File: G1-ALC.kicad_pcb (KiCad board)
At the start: 2 copper layers, 100 x 100.1 mm, 89 parts, among them J101 Conn_01x03_Pin, J102 330 VAC In, J103 G1 conn., J104 105VAC in, J105 Conn_01x03_Pin, J107 Conn_01x05_Pin, J108 G2 Control board interconnect, Q101 TIP122, U101 LM7812_TO220, U102 LM324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

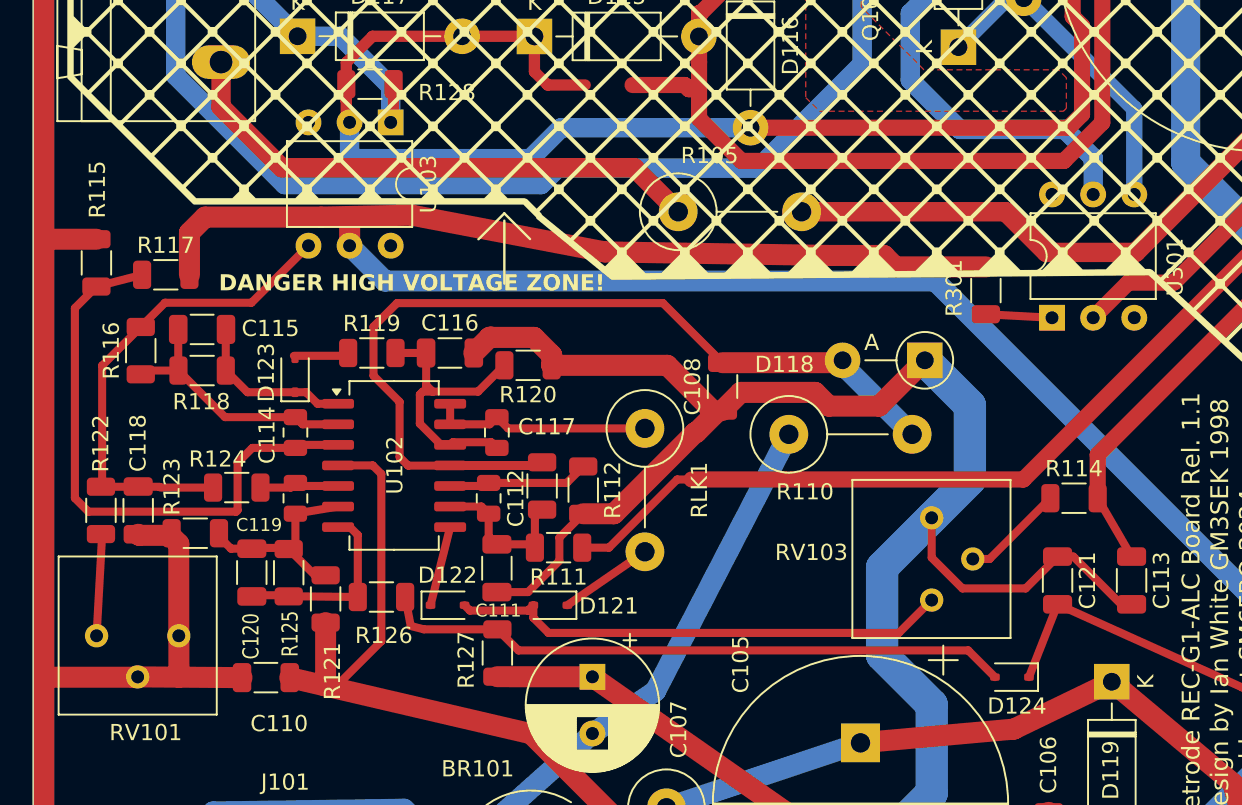
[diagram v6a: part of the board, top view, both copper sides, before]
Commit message: Moved cold end of R115 to CLASS_AB1_L instead of GND. The intent is to turn off ALC in case we want to run the PA in class C.
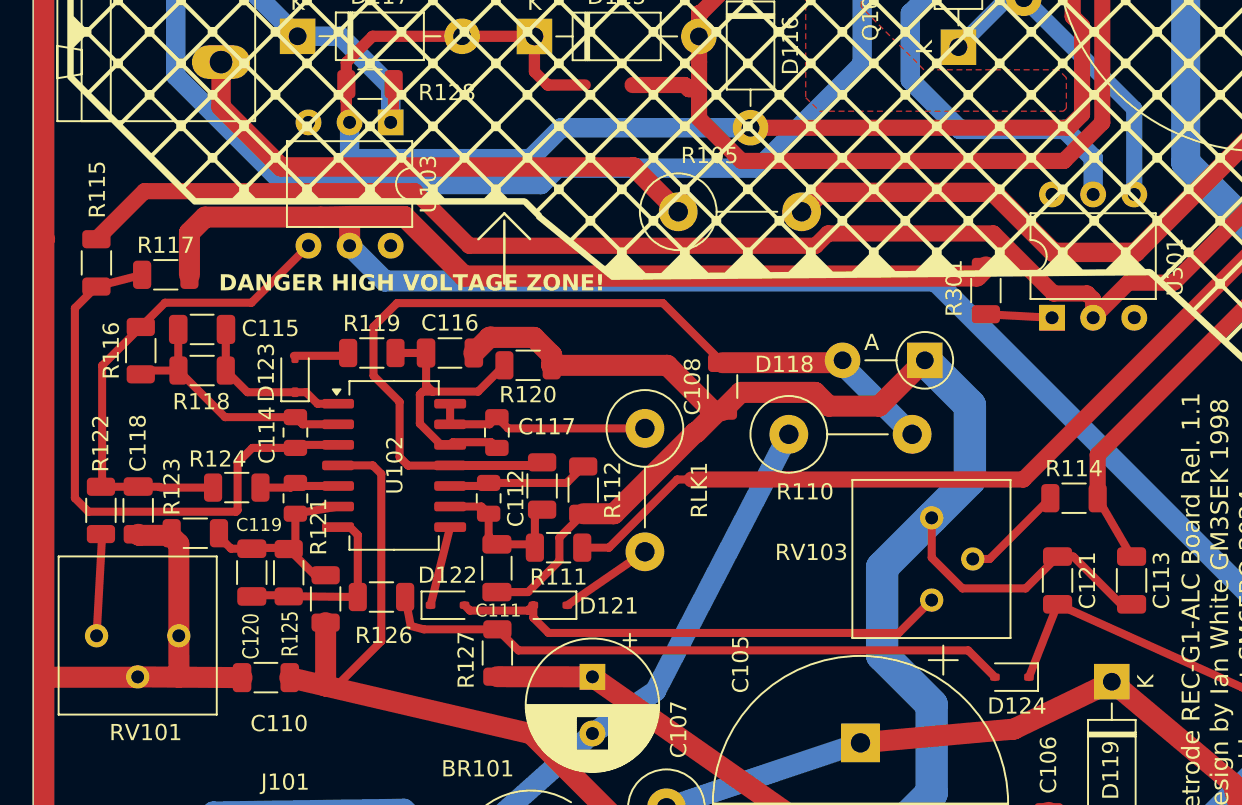
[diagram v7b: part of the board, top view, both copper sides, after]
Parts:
- turned R121 to -90 degrees
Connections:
- R115 pad 1: GNDPWR -> /Class AB1_L
- R121 pad 1: +12V Reg -> Net-(U102B--)
- R121 pad 2: Net-(U102B--) -> +12V Reg
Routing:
- net /Class AB1_L: track 45.9 -> 113.2 mm
- net GNDPWR: track 992.8 -> 989.6 mm
- net +12V Reg: track 285.2 -> 286.4 mm
- net Net-(C103-Pad2): track 81.2 -> 82.2 mm
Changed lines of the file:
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@@
 	(footprint "Resistor_SMD:R_1206_3216Metric"
 		(layer "F.Cu")
-		(at 68.1 101.67 90)
+		(at 68.1 101.67 -90)
 		(descr "Resistor SMD 1206 (3216 Metric), square (rectangular) end terminal, IPC_7351 nominal, (Body size source: IPC-SM-782 page 72, https://www.pcb-3d.com/wordpress/wp-content/uploads/ipc-sm-782a_amendment_1_and_2.pdf), generated with kicad-footprint-generator")
 		(tags "resistor")
@@
 		)
 		(property "Footprint" "Resistor_SMD:R_1206_3216Metric"
-			(at 0 0 90)
+			(at 0 0 -90)
 			(unlocked yes)
 			(layer "F.Fab")
@@
 		)
 		(property "Datasheet" ""
-			(at 0 0 90)
+			(at 0 0 -90)
 			(unlocked yes)
 			(layer "F.Fab")
@@
 		)
 		(property "Description" ""
-			(at 0 0 90)
+			(at 0 0 -90)
 			(unlocked yes)
 			(layer "F.Fab")
@@
 		)
 		(property "Notes" ""
-			(at 0 0 0)
+			(at 0 0 180)
 			(layer "F.Fab")
 			(hide yes)
@@
 		)
 		(property "Order #" "40818410"
-			(at 0 0 0)
+			(at 0 0 180)
 			(layer "F.Fab")
 			(hide yes)
@@
 		)
 		(property "Supplier" "Electrokit"
-			(at 0 0 0)
+			(at 0 0 180)
 			(layer "F.Fab")
 			(hide yes)
@@
 		(attr smd)
 		(fp_line
-			(start -0.727064 -0.91)
-			(end 0.727064 -0.91)
+			(start -0.727064 0.91)
+			(end 0.727064 0.91)
 			(stroke
 				(width 0.12)
@@
 		)
 		(fp_line
-			(start -0.727064 0.91)
-			(end 0.727064 0.91)
+			(start -0.727064 -0.91)
+			(end 0.727064 -0.91)
 			(stroke
 				(width 0.12)
@@
 		)
 		(fp_line
-			(start 2.28 -1.12)
-			(end 2.28 1.12)
+			(start -2.28 1.12)
+			(end -2.28 -1.12)
 			(stroke
 				(width 0.05)
@@
 		)
 		(fp_line
-			(start -2.28 -1.12)
-			(end 2.28 -1.12)
+			(start 2.28 1.12)
+			(end -2.28 1.12)
 			(stroke
 				(width 0.05)
@@
 		)
 		(fp_line
-			(start 2.28 1.12)
-			(end -2.28 1.12)
+			(start -2.28 -1.12)
+			(end 2.28 -1.12)
 			(stroke
 				(width 0.05)
@@
 		)
 		(fp_line
-			(start -2.28 1.12)
-			(end -2.28 -1.12)
+			(start 2.28 -1.12)
+			(end 2.28 1.12)
 			(stroke
 				(width 0.05)
@@
 		)
 		(fp_line
-			(start 1.6 -0.8)
-			(end 1.6 0.8)
+			(start -1.6 0.8)
+			(end -1.6 -0.8)
 			(stroke
 				(width 0.1)
@@
 		)
 		(fp_line
-			(start -1.6 -0.8)
-			(end 1.6 -0.8)
+			(start 1.6 0.8)
+			(end -1.6 0.8)
 			(stroke
 				(width 0.1)
@@
 		)
 		(fp_line
-			(start 1.6 0.8)
-			(end -1.6 0.8)
+			(start -1.6 -0.8)
+			(end 1.6 -0.8)
 			(stroke
 				(width 0.1)
@@
 		)
 		(fp_line
-			(start -1.6 0.8)
-			(end -1.6 -0.8)
+			(start 1.6 -0.8)
+			(end 1.6 0.8)
 			(stroke
 				(width 0.1)
@@
 		)
 		(pad "1" smd roundrect
-			(at -1.4625 0 90)
+			(at -1.4625 0 270)
 			(size 1.125 1.75)
 			(layers "F.Cu" "F.Paste" "F.Mask")
 			(roundrect_rratio 0.2222222222)
-			(net 10 "+12V Reg")
+			(net 24 "Net-(U102B--)")
 			(pintype "passive")
 		)
 		(pad "2" smd roundrect
-			(at 1.4625 0 90)
+			(at 1.4625 0 270)
 			(size 1.125 1.75)
 			(layers "F.Cu" "F.Paste" "F.Mask")
 			(roundrect_rratio 0.2222222222)
-			(net 24 "Net-(U102B--)")
+			(net 10 "+12V Reg")
 			(pintype "passive")
 		)
@@
 			(layers "F.Cu" "F.Paste" "F.Mask")
 			(roundrect_rratio 0.2222222222)
-			(net 11 "GNDPWR")
+			(net 49 "/Class AB1_L")
 			(pintype "passive")
 		)
@@
 	)
 	(segment
-		(start 97.505 77.75)
-		(end 110.11 77.75)
+		(start 130.839775 61.384316)
+		(end 130.839775 47.630225)
 		(width 1.2)
 		(layer "F.Cu")
@@
 	)
 	(segment
-		(start 130.839775 61.384316)
-		(end 130.839775 47.630225)
+		(start 130.999775 47.630225)
+		(end 133.46 45.17)
 		(width 1.2)
 		(layer "F.Cu")
@@
 	)
 	(segment
-		(start 130.999775 47.630225)
-		(end 133.46 45.17)
+		(start 113.06132 80.26)
+		(end 118.14 80.26)
 		(width 1.2)
 		(layer "F.Cu")
@@
 	)
 	(segment
-		(start 110.11 77.75)
-		(end 112.62 80.26)
+		(start 97.505 77.75)
+		(end 98.705 76.55)
 		(width 1.2)
 		(layer "F.Cu")
@@
 	)
 	(segment
-		(start 118.14 80.26)
-		(end 130.839775 67.560225)
+		(start 109.35132 76.55)
+		(end 113.06132 80.26)
+		(width 1.2)
+		(layer "F.Cu")
+		(net 8)
+	)
+	(segment
+		(start 98.705 76.55)
+		(end 109.35132 76.55)
 		(width 1.2)
 		(layer "F.Cu")
@@
 	)
 	(segment
-		(start 112.62 80.26)
-		(end 118.14 80.26)
+		(start 118.14 80.26)
+		(end 130.839775 67.560225)
 		(width 1.2)
 		(layer "F.Cu")
@@
 	)
 	(segment
-		(start 102.587732 80.45)
-		(end 103.295232 81.1575)
-		(width 1.3)
-		(layer "F.Cu")
-		(net 10)
-	)
-	(segment
 		(start 115.805476 117.807)
 		(end 116.669476 116.943)
@@
 	(segment
 		(start 69.59 78.041598)
-		(end 73.42 77.96)
+		(end 72.969567 78.041598)
 		(width 1.3)
 		(layer "F.Cu")
@@
 	)
 	(segment
+		(start 72.969567 78.041598)
+		(end 76.647969 81.72)
+		(width 1.3)
+		(layer "F.Cu")
+		(net 10)
+	)
+	(segment
 		(start 112.776 117.807)
 		(end 115.805476 117.807)
@@
 	)
 	(segment
+		(start 108.3275 81.72)
+		(end 108.89 81.1575)
+		(width 1.3)
+		(layer "F.Cu")
+		(net 10)
+	)
+	(segment
 		(start 68.1 103.1325)
 		(end 68.1 107.045669)
@@
 	)
 	(segment
-		(start 73.42 77.96)
-		(end 85.34 80.23)
+		(start 76.647969 81.72)
+		(end 108.3275 81.72)
 		(width 1.3)
 		(layer "F.Cu")
@@
 	)
 	(segment
-		(start 99.33 80.45)
-		(end 102.587732 80.45)
-		(width 1.3)
-		(layer "F.Cu")
-		(net 10)
-	)
-	(segment
-		(start 85.34 80.23)
-		(end 99.33 80.45)
-		(width 1.3)
-		(layer "F.Cu")
-		(net 10)
-	)
-	(segment
-		(start 103.295232 81.1575)
-		(end 108.89 81.1575)
-		(width 1.3)
-		(layer "F.Cu")
-		(net 10)
-	)
-	(segment
 		(start 137.11 98.32)
 		(end 143.2975 98.32)
@@
 	)
 	(segment
-		(start 53.94 79.447367)
-		(end 50.738633 79.447367)
-		(width 1.3)
-		(layer "F.Cu")
-		(net 11)
-	)
-	(segment
 		(start 116 124.426)
 		(end 144.824 124.426)
@@
 	)
 	(segment
-		(start 87.165 75.03)
-		(end 89.885 77.75)
+		(start 61.6387 68.5038)
+		(end 61.6387 71.2687)
 		(width 1.2)
 		(layer "F.Cu")
@@
 	)
 	(segment
-		(start 65.4 75.03)
-		(end 87.165 75.03)
+		(start 87.115 74.98)
+		(end 89.885 77.75)
 		(width 1.2)
 		(layer "F.Cu")
@@
 	)
 	(segment
-		(start 61.6387 68.5038)
-		(end 61.6387 71.2687)
+		(start 65.35 74.98)
+		(end 87.115 74.98)
 		(width 1.2)
 		(layer "F.Cu")
@@
 	(segment
 		(start 61.6387 71.2687)
-		(end 65.4 75.03)
+		(end 65.35 74.98)
 		(width 1.2)
 		(layer "F.Cu")
@@
 	)
 	(segment
+		(start 113.07 82.8)
+		(end 109.362425 79.092425)
+		(width 1)
+		(layer "F.Cu")
+		(net 49)
+	)
+	(segment
+		(start 115.515 84.3)
+		(end 115.515 83.16863)
+		(width 1)
+		(layer "F.Cu")
+		(net 49)
+	)
+	(segment
+		(start 98.374849 79.85)
+		(end 76.97 79.85)
+		(width 1)
+		(layer "F.Cu")
+		(net 49)
+	)
+	(segment
 		(start 135.62 67.01)
 		(end 120.5 82.13)
@@
 	)
 	(segment
+		(start 76.97 79.85)
+		(end 73.6 76.48)
+		(width 1)
+		(layer "F.Cu")
+		(net 49)
+	)
+	(segment
+		(start 115.515 83.16863)
+		(end 115.14637 82.8)
+		(width 1)
+		(layer "F.Cu")
+		(net 49)
+	)
+	(segment
+		(start 115.14637 82.8)
+		(end 113.07 82.8)
+		(width 1)
+		(layer "F.Cu")
+		(net 49)
+	)
+	(segment
+		(start 56.907367 76.48)
+		(end 53.94 79.447367)
+		(width 1)
+		(layer "F.Cu")
+		(net 49)
+	)
+	(segment
 		(start 138.77 54.3)
 		(end 135.62 57.45)
@@
 	)
 	(segment
+		(start 73.6 76.48)
+		(end 56.907367 76.48)
+		(width 1)
+		(layer "F.Cu")
+		(net 49)
+	)
+	(segment
+		(start 109.362425 79.092425)
+		(end 99.132424 79.092425)
+		(width 1)
+		(layer "F.Cu")
+		(net 49)
+	)
+	(segment
 		(start 120.5 82.13)
 		(end 117.685 82.13)
@@
 		(width 1)
 		(layer "F.Cu")
+		(net 49)
+	)
+	(segment
+		(start 99.132424 79.092425)
+		(end 98.374849 79.85)
+		(width 1)
+		(layer "F.Cu")

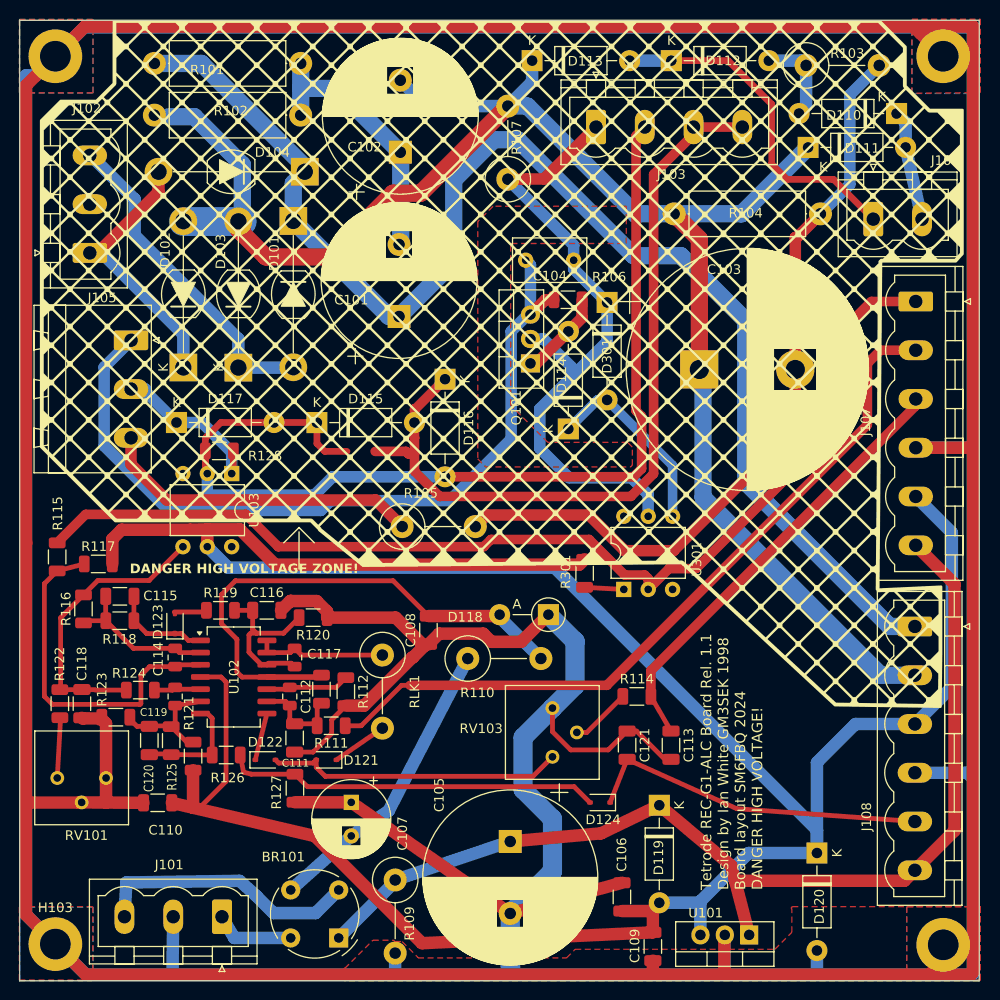
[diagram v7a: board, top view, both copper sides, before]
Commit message: Updated format to KiCad 9. Included footprints etc.
Standardized PCB layers, updated property formatting, and adjusted net assignments. Added some DigiKey, Electrokit, and Mouser component part numbers.
Reduced font sizes for better readability and incorporated embedded font settings.
Removed the sequencer from the schematic which wasn't really meant to be there.
Revised and excluded drc and erc warnings and exclusions.
Included footprints into the project library that formerly was defined outside of the project.
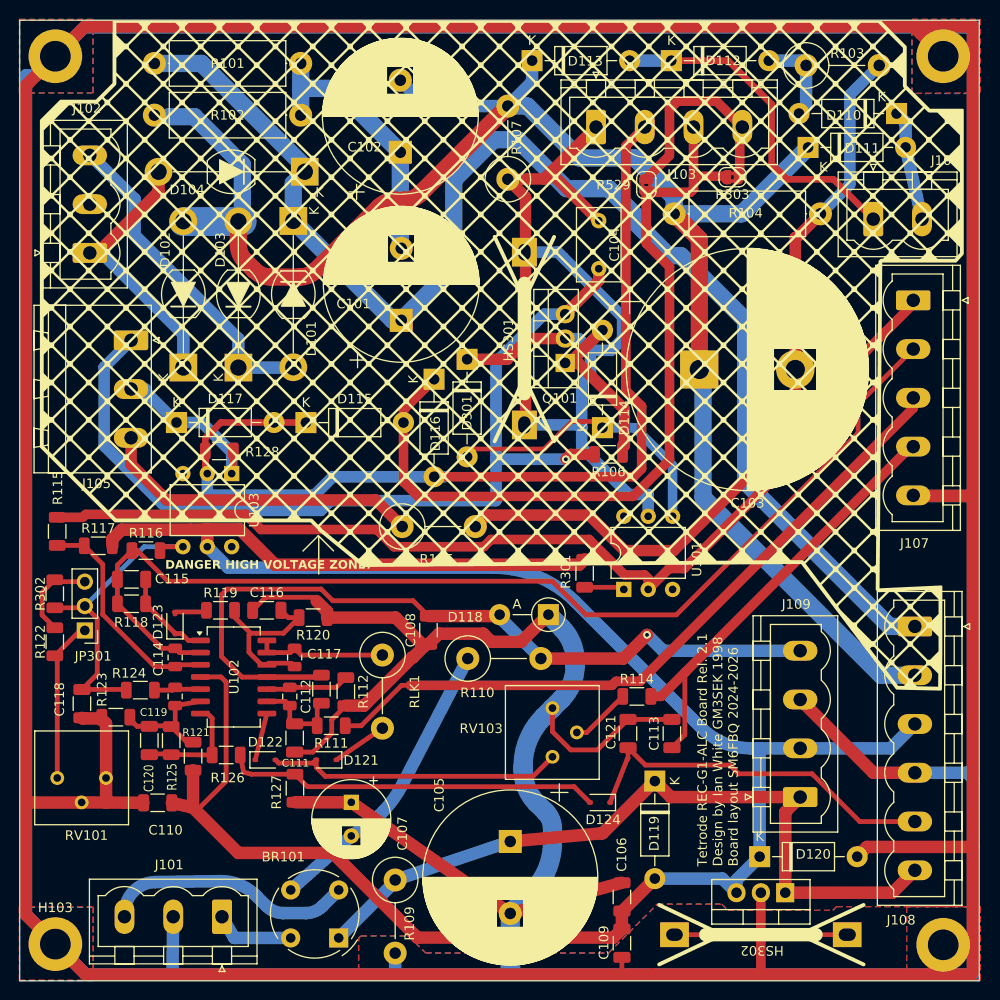
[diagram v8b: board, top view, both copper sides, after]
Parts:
- added HS301: Heatsink_Pad_2Pin, Project_library:6025DG_Cooler, F.Cu at (102.6, 58.2)
- added HS302: Heatsink_Pad_2Pin, Project_library:6025DG_Cooler, F.Cu at (127.3, 120.3)
- added J109: G1 conn., Connector_Phoenix_MSTB:PhoenixContact_MSTBVA_2,5_4-G-5,08_1x04_P5.08mm_Vertical, F.Cu at (131.3, 105.9)
- added JP301: ALC tune, Connector_PinHeader_2.54mm:PinHeader_1x03_P2.54mm_Vertical, F.Cu at (56.8, 88.6)
- added R302: 560R, Resistor_SMD:R_1206_3216Metric, F.Cu at (53.7, 84.8)
- added R303: 0, Jumper:SolderJumper-2_P1.3mm_Bridged2Bar_RoundedPad1.0x1.5mm, F.Cu at (124.3, 41.4)
- added R529: 0, Jumper:SolderJumper-2_P1.3mm_Bridged2Bar_RoundedPad1.0x1.5mm, F.Cu at (115.3, 42.2)
- D101, D102, D103, D104: footprint Diode_THT_AKL:D_SOD-64_P15.24mm_big_holes_Horizontal -> Project_library:D_SOD-64_P15.24mm_big_holes_Horizontal
- J102: value 330 VAC In -> 330VAC
- J107: footprint Connector_Phoenix_MSTB:PhoenixContact_MSTBVA_2,5_6-G-5,08_1x06_P5.08mm_Vertical -> Connector_Phoenix_MSTB:PhoenixContact_MSTBVA_2,5_5-G-5,08_1x05_P5.08mm_Vertical
- Q101, U101: footprint Package_TO_SOT_THT:TO-220-3_Vertical_Cooler -> Package_TO_SOT_THT:TO-220-3_Vertical
- R126: value 100k -> 39k
- moved R106 16.7 mm to (111.4, 70.2)
- moved D301 15.7 mm to (96.6, 60.3)
- moved R116 8.91 mm to (63.2, 80.3), turned to 0 degrees
- moved R122 6.47 mm to (53.7, 89.8)
- moved D120 5.98 mm to (127.1, 112.1), turned to 0 degrees
- moved U101 5.79 mm to (129.8, 115.9)
- moved C104 4.87 mm to (110.4, 45.9), turned to -90 degrees
- moved Q101 3.61 mm to (106.9, 60.7)
- moved D114 3.56 mm to (110.7, 67.5)
- moved C109 3.24 mm to (112.8, 121.2)
- moved R115 2.66 mm to (53.9, 78.3)
- moved D119 2.56 mm to (116.2, 104.3)
- moved C115 2.15 mm to (61.7, 83.3)
- moved R118 2.15 mm to (61.7, 85.8)
- moved R117 1.89 mm to (58.2, 79.8)
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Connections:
- C105 pad 2: GNDPWR -> GND
- C106 pad 1: +12V Reg -> +12V
- C106 pad 2: GNDPWR -> GND
- C107 pad 1: GNDPWR -> GND
- C108 pad 1: GNDPWR -> GND
- C109 pad 1: +12V Reg -> +12V
- C109 pad 2: GNDPWR -> GND
- C110 pad 1: +12V Reg -> +12V
- C110 pad 2: GNDPWR -> GND
- C111 pad 2: GNDPWR -> GND
- C113 pad 2: GNDPWR -> GND
- C114 pad 2: Net-(U102A--) -> /Ig1
- C115 pad 1: Net-(U102A--) -> /Ig1
- C116 pad 1: Net-(U102D-+) -> GND
- C116 pad 2: GNDPWR -> Net-(U102D-+)
- C118 pad 1: Net-(C118-Pad1) -> Net-(JP301-C)
- C118 pad 2: GNDPWR -> GND
- C121 pad 1: GNDPWR -> GND
- D115 pad 2: /G1 -> /G1 meter -
- D116 pad 1: /G1 -> /G1 meter -
- D118 pad 1: GNDPWR -> GND
- D119 pad 2: +12V Reg -> +12V
- D120 pad 1: +12V Reg -> +12V
- D120 pad 2: GNDPWR -> GND
- H101 pad 1: GNDPWR -> GND
- H102 pad 1: GNDPWR -> GND
- H103 pad 1: GNDPWR -> GND
- H104 pad 1: GNDPWR -> GND
- J101 pad 2: GNDPWR -> GND
- J103 pad 3: /G1 -> /G1 meter -
- J107 pad 2: /Inhibit -> /Ig1
- J107 pad 3: /ALC -> /Inhibit
- J107 pad 4: GNDPWR -> /ALC
- J107 pad 5: +12V Reg -> GND
- J108 pad 3: +12V Reg -> +12V
- J108 pad 4: GNDPWR -> GND
- R109 pad 2: GNDPWR -> GND
- R112 pad 2: GNDPWR -> GND
- R116 pad 1: Net-(U102A--) -> /Ig1
- R116 pad 2: Net-(C118-Pad1) -> Net-(JP301-C)
- R117 pad 2: +12V Reg -> +12V
- R118 pad 1: Net-(U102A--) -> /Ig1
- R120 pad 1: GNDPWR -> GND
- R121 pad 2: +12V Reg -> +12V
- R122 pad 1: Net-(C118-Pad1) -> Net-(JP301-B)
- R123 pad 1: GNDPWR -> GND
- R124 pad 1: Net-(C118-Pad1) -> Net-(JP301-C)
- R127 pad 1: GNDPWR -> GND
- R301 pad 1: +12V Reg -> +12V
- RV101 pad 2: GNDPWR -> GND
- RV101 pad 3: GNDPWR -> GND
- RV103 pad 3: GNDPWR -> GND
- U101 pad 2: GNDPWR -> GND
- U101 pad 3: +12V Reg -> +12V
- U102 pad 2: Net-(U102A--) -> /Ig1
- U102 pad 4: +12V Reg -> +12V
- U103 pad 4: Net-(C118-Pad1) -> Net-(JP301-C)
- U103 pad 5: +12V Reg -> +12V
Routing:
- net GND: track 0.00 -> 1035.4 mm
- net GNDPWR: track 989.6 -> 0.00 mm
- net +12V Reg: track 286.4 -> 0.00 mm
- net +12V: track 0.00 -> 242.0 mm
- net /Ig1: track 0.00 -> 114.3 mm
- net /G1 meter -: track 0.00 -> 85.8 mm
- net /G1: track 84.4 -> 22.6 mm
- net /G1 Switch: track 68.8 -> 106.1 mm
- net Net-(JP301-C): track 0.00 -> 33.7 mm
- net +24V Unreg: track 110.9 -> 79.2 mm
- net Net-(C118-Pad1): track 30.1 -> 0.00 mm
- net -12V: track 60.1 -> 88.1 mm, vias 0 -> 1
- net Net-(U102A--): track 15.9 -> 0.00 mm
- net /RV102 Cold: track 83.1 -> 96.5 mm, vias 0 -> 1
- net Net-(U102A-+): track 36.3 -> 23.0 mm
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- added copper zone on B.Cu, net GND
- added copper zone on F.Cu, net GND
- removed copper zone on F.Cu, net (none)
- removed copper zone on B.Cu, net GNDPWR
- removed copper zone on F.Cu, net GNDPWR
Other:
- board text added: "-12V"
- board text added: "ALC"
- board text added: "Class AB1_L"
- board text added: "G1 trip"
- board text added: "Ig1"
- board text added: "Inhibit"
- board text added: "Tetrode REC-G1-ALC Board Rel. 2.1 Design by Ian White GM3SEK 1998 Board layout SM6FBQ 2024-2026"
- board text removed: "ALC out"
- board text removed: "Class-AB1_L"
- board text removed: "G1 Current trip"
- board text removed: "Inh in"
- board text removed: "Tetrode REC-G1-ALC Board Rel. 1.1 Design by Ian White GM3SEK 1998 Board layout SM6FBQ 2024 DANGER HIGH VOLTAGE!"
